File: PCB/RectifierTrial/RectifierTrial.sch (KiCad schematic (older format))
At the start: 9 parts, among them J1 Conn_01x03, J2 Conn_01x02

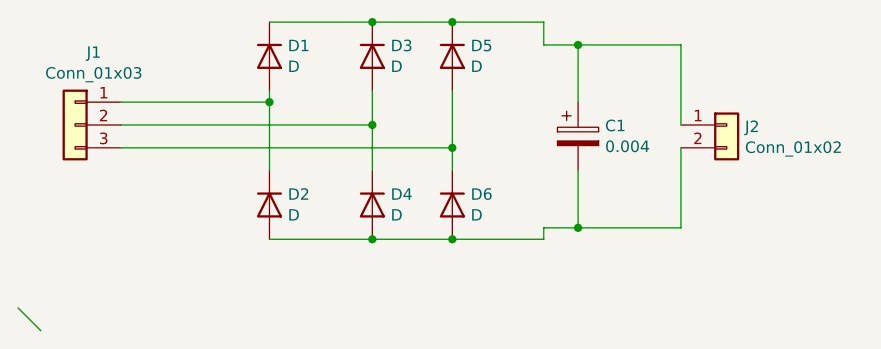
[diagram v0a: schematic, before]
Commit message: Rectifier PCB is added
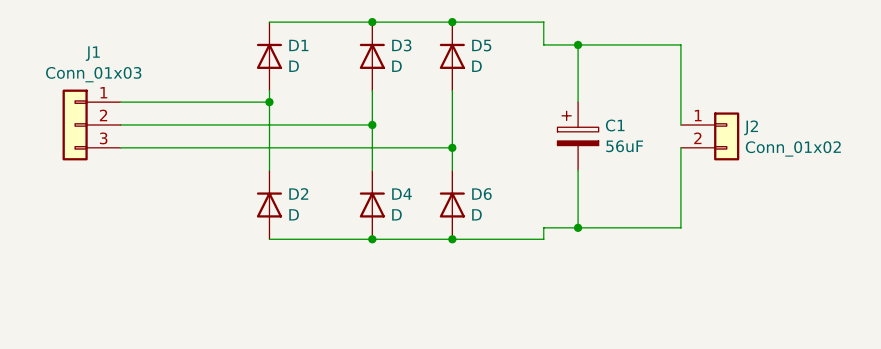
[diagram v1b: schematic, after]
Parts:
- C1: value 0.004 -> 56uF; footprint Capacitor_THT:CP_Radial_D12.5mm_P2.50mm -> Capacitor_THT:CP_Radial_D22.0mm_P10.00mm_SnapIn
- D1, D2, D3, D4, D5, D6: footprint Diode_THT:D_5KP_P12.70mm_Horizontal -> Diode_THT:D_DO-15_P10.16mm_Horizontal
- J2: footprint Connector_PinSocket_2.54mm:PinSocket_1x02_P2.54mm_Horizontal -> Connector_Phoenix_MC_HighVoltage:PhoenixContact_MCV_1,5_2-G-5.08_1x02_P5.08mm_Vertical
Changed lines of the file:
@@
 encoding utf-8
 Sheet 1 1
-Title ""
-Date ""
+Title "Diode Rectifier"
+Date "2020-12-19"
 Rev ""
 Comp ""
@@
 P 6400 3000
 F 0 "C1" H 6518 3046 50  0000 L CNN
-F 1 "0.004" H 6518 2955 50  0000 L CNN
-F 2 "Capacitor_THT:CP_Radial_D12.5mm_P2.50mm" H 6438 2850 50  0001 C CNN
+F 1 "56uF" H 6518 2955 50  0000 L CNN
+F 2 "Capacitor_THT:CP_Radial_D22.0mm_P10.00mm_SnapIn" H 6438 2850 50  0001 C CNN
 F 3 "~" H 6400 3000 50  0001 C CNN
 	1    6400 3000
@@
 F 0 "D1" V 5004 2730 50  0000 L CNN
 F 1 "D" V 5095 2730 50  0000 L CNN
-F 2 "Diode_THT:D_5KP_P12.70mm_Horizontal" H 5050 2650 50  0001 C CNN
+F 2 "Diode_THT:D_DO-15_P10.16mm_Horizontal" H 5050 2650 50  0001 C CNN
 F 3 "~" H 5050 2650 50  0001 C CNN
 	1    5050 2650
@@
 F 0 "D3" V 5454 2730 50  0000 L CNN
 F 1 "D" V 5545 2730 50  0000 L CNN
-F 2 "Diode_THT:D_5KP_P12.70mm_Horizontal" H 5500 2650 50  0001 C CNN
+F 2 "Diode_THT:D_DO-15_P10.16mm_Horizontal" H 5500 2650 50  0001 C CNN
 F 3 "~" H 5500 2650 50  0001 C CNN
 	1    5500 2650
@@
 F 0 "D5" V 5804 2730 50  0000 L CNN
 F 1 "D" V 5895 2730 50  0000 L CNN
-F 2 "Diode_THT:D_5KP_P12.70mm_Horizontal" H 5850 2650 50  0001 C CNN
+F 2 "Diode_THT:D_DO-15_P10.16mm_Horizontal" H 5850 2650 50  0001 C CNN
 F 3 "~" H 5850 2650 50  0001 C CNN
 	1    5850 2650
@@
 F 0 "D2" V 5004 3380 50  0000 L CNN
 F 1 "D" V 5095 3380 50  0000 L CNN
-F 2 "Diode_THT:D_5KP_P12.70mm_Horizontal" H 5050 3300 50  0001 C CNN
+F 2 "Diode_THT:D_DO-15_P10.16mm_Horizontal" H 5050 3300 50  0001 C CNN
 F 3 "~" H 5050 3300 50  0001 C CNN
 	1    5050 3300
@@
 F 0 "D4" V 5454 3380 50  0000 L CNN
 F 1 "D" V 5545 3380 50  0000 L CNN
-F 2 "Diode_THT:D_5KP_P12.70mm_Horizontal" H 5500 3300 50  0001 C CNN
+F 2 "Diode_THT:D_DO-15_P10.16mm_Horizontal" H 5500 3300 50  0001 C CNN
 F 3 "~" H 5500 3300 50  0001 C CNN
 	1    5500 3300
@@
 F 0 "D6" V 5804 3380 50  0000 L CNN
 F 1 "D" V 5895 3380 50  0000 L CNN
-F 2 "Diode_THT:D_5KP_P12.70mm_Horizontal" H 5850 3300 50  0001 C CNN
+F 2 "Diode_THT:D_DO-15_P10.16mm_Horizontal" H 5850 3300 50  0001 C CNN
 F 3 "~" H 5850 3300 50  0001 C CNN
 	1    5850 3300
@@
 	-1   0    0    -1
 $EndComp
-Entry Wire Line
-	3950 3750 4050 3850
 $Comp
 L Connector_Generic:Conn_01x02 J2
@@
 F 0 "J2" H 7130 2942 50  0000 L CNN
 F 1 "Conn_01x02" H 7130 2851 50  0000 L CNN
-F 2 "Connector_PinSocket_2.54mm:PinSocket_1x02_P2.54mm_Horizontal" H 7050 2950 50  0001 C CNN
+F 2 "Connector_Phoenix_MC_HighVoltage:PhoenixContact_MCV_1,5_2-G-5.08_1x02_P5.08mm_Vertical" H 7050 2950 50  0001 C CNN
 F 3 "~" H 7050 2950 50  0001 C CNN
 	1    7050 2950
